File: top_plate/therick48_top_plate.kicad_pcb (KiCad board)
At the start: 2 copper layers, 227.2 x 75.2 mm, 54 parts, among them U1 HOLE, U10 HOLE, U11 HOLE, U12 HOLE, U13 HOLE, U14 HOLE, U15 HOLE, U16 HOLE, U17 HOLE, U18 HOLE, U19 HOLE, U2 HOLE, U20 HOLE, U21 HOLE, U22 HOLE, U23 HOLE, U24 HOLE, U25 HOLE, U26 HOLE, U27 HOLE, U28 HOLE, U29 HOLE, U3 HOLE, U30 HOLE, U31 HOLE, U32 HOLE, U33 HOLE, U34 HOLE, U35 HOLE, U36 HOLE, U37 HOLE, U38 HOLE, U39 HOLE, U4 HOLE, U40 HOLE, U41 HOLE, U42 HOLE, U43 HOLE, U44 HOLE, U45 HOLE, U46 HOLE, U47 HOLE, U48 HOLE, U5 HOLE, U6 HOLE, U7 HOLE, U8 HOLE, U9 HOLE

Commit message: Add Gerbers
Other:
- board text added: "therick48 Rev 1.0"
- board text removed: "therick_19mm"
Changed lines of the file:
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@@
   )
   (gr_line (start 273.6 38.38) (end 273.6 106.78) (layer Edge.Cuts) (width 0.05))
-  (gr_text therick_19mm (at 254.98 91.58) (layer B.SilkS)
+  (gr_text "therick48 Rev 1.0" (at 254.98 91.58) (layer B.SilkS)
     (effects (font (size 1.5 1.5) (thickness 0.2)) (justify mirror))
   )

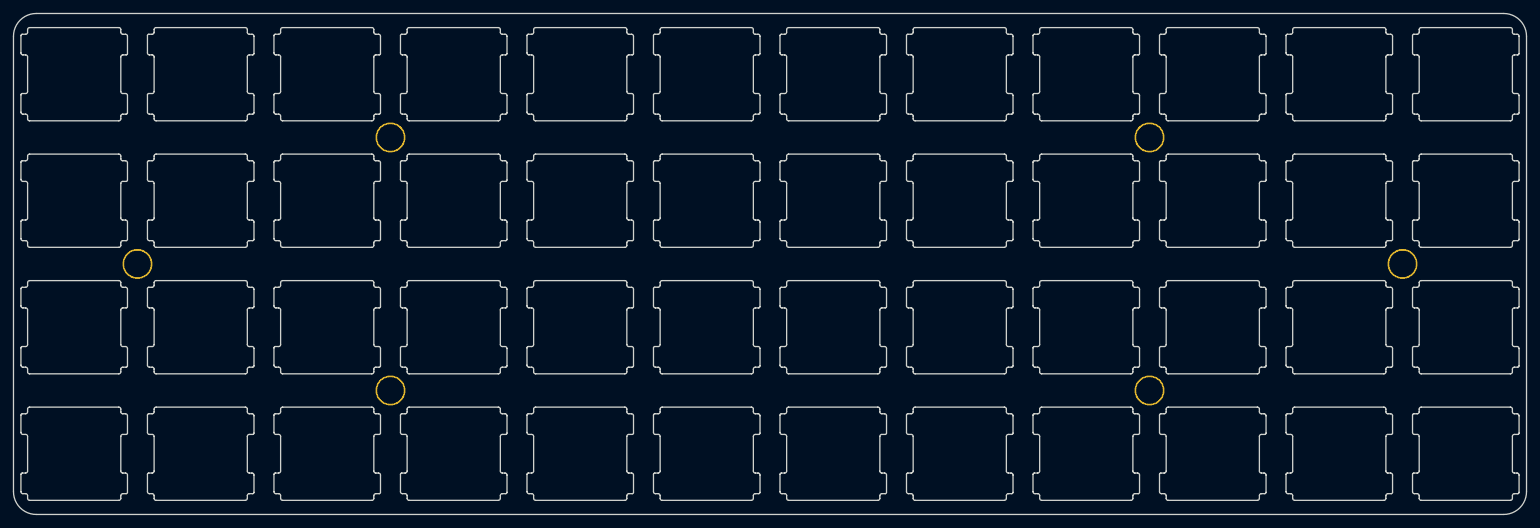
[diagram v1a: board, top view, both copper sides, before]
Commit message: Updated mounting holes
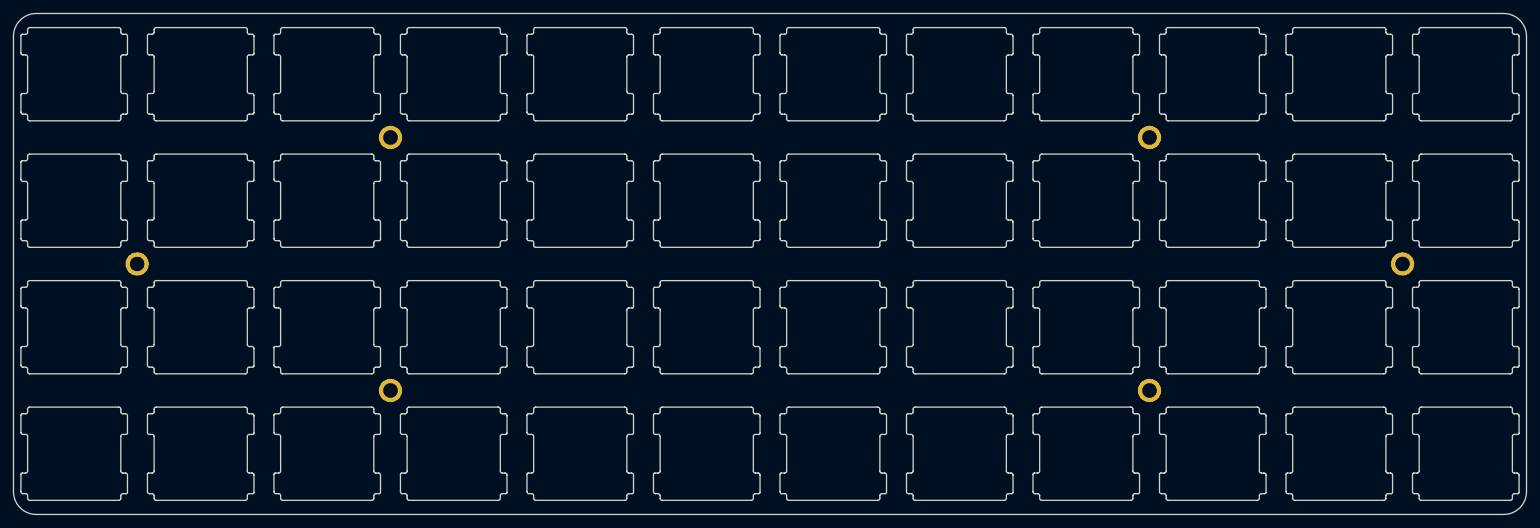
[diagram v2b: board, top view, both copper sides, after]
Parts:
- H1, H2, H3, H4, H5, H6: footprint random-keyboard-parts:plate_hole_4mm_tht -> random-keyboard-parts:Generic-Mounthole
- moved H2 2.03 mm to (103.0, 53.6)
- moved H4 2.03 mm to (217.0, 53.6)
- moved H3 2.03 mm to (103.0, 91.6)
- moved H5 2.03 mm to (217.0, 91.6)
- moved H6 2.03 mm to (255.0, 72.6)
- moved H1 2.03 mm to (64.9, 72.6)
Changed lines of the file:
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@@
     (solder_mask_min_width 0.25)
     (aux_axis_origin 0 0)
-    (visible_elements FFFFEF7F)
+    (visible_elements FFFFFF7F)
     (pcbplotparams
       (layerselection 0x010fc_ffffffff)
@@
     (uvia_drill 0.1)
   )
+  (module random-keyboard-parts:Generic-Mounthole locked (layer F.Cu)
+    (at 254.98 72.58)
+    (attr virtual)
+    (fp_text reference H6 (at 0 2) (layer Dwgs.User)
+      (effects (font (size 1 1) (thickness 0.15)))
+    )
+    (fp_text value MountingHole (at 0 -2) (layer Dwgs.User)
+      (effects (font (size 1 1) (thickness 0.15)))
+    )
+    (pad 1 thru_hole circle (at 0 0) (size 3.5 3.5) (drill 2.2) (layers *.Cu *.Mask))
+  )
+  (module random-keyboard-parts:Generic-Mounthole locked (layer F.Cu)
+    (at 216.98 91.58)
+    (attr virtual)
+    (fp_text reference H5 (at 0 2) (layer Dwgs.User)
+      (effects (font (size 1 1) (thickness 0.15)))
+    )
+    (fp_text value MountingHole (at 0 -2) (layer Dwgs.User)
+      (effects (font (size 1 1) (thickness 0.15)))
+    )
+    (pad 1 thru_hole circle (at 0 0) (size 3.5 3.5) (drill 2.2) (layers *.Cu *.Mask))
+  )
+  (module random-keyboard-parts:Generic-Mounthole locked (layer F.Cu)
+    (at 216.98 53.58)
+    (attr virtual)
+    (fp_text reference H4 (at 0 2) (layer Dwgs.User)
+      (effects (font (size 1 1) (thickness 0.15)))
+    )
+    (fp_text value MountingHole (at 0 -2) (layer Dwgs.User)
+      (effects (font (size 1 1) (thickness 0.15)))
+    )
+    (pad 1 thru_hole circle (at 0 0) (size 3.5 3.5) (drill 2.2) (layers *.Cu *.Mask))
+  )
+  (module random-keyboard-parts:Generic-Mounthole locked (layer F.Cu)
+    (at 102.98 91.58)
+    (attr virtual)
+    (fp_text reference H3 (at 0 2) (layer Dwgs.User)
+      (effects (font (size 1 1) (thickness 0.15)))
+    )
+    (fp_text value MountingHole (at 0 -2) (layer Dwgs.User)
+      (effects (font (size 1 1) (thickness 0.15)))
+    )
+    (pad 1 thru_hole circle (at 0 0) (size 3.5 3.5) (drill 2.2) (layers *.Cu *.Mask))
+  )
+  (module random-keyboard-parts:Generic-Mounthole locked (layer F.Cu)
+    (at 102.98 53.58)
+    (attr virtual)
+    (fp_text reference H2 (at 0 2) (layer Dwgs.User)
+      (effects (font (size 1 1) (thickness 0.15)))
+    )
+    (fp_text value MountingHole (at 0 -2) (layer Dwgs.User)
+      (effects (font (size 1 1) (thickness 0.15)))
+    )
+    (pad 1 thru_hole circle (at 0 0) (size 3.5 3.5) (drill 2.2) (layers *.Cu *.Mask))
+  )
+  (module random-keyboard-parts:Generic-Mounthole locked (layer F.Cu)
+    (at 64.9292 72.58)
+    (attr virtual)
+    (fp_text reference H1 (at 0 2) (layer Dwgs.User)
+      (effects (font (size 1 1) (thickness 0.15)))
+    )
+    (fp_text value MountingHole (at 0 -2) (layer Dwgs.User)
+      (effects (font (size 1 1) (thickness 0.15)))
+    )
+    (pad 1 thru_hole circle (at 0 0) (size 3.5 3.5) (drill 2.2) (layers *.Cu *.Mask))
+  )
   (module random-keyboard-parts:MX100_slot (layer F.Cu)
     (at 264.48 63.08)
@@
     (fp_arc (start -7.8 -5.8) (end -7.8 -6) (angle -90) (layer Edge.Cuts) (width 0.1))
   )
-  (module random-keyboard-parts:plate_hole_4mm_tht locked (layer F.Cu)
-    (at 64.9292 74.612)
-    (fp_text reference H1 (at 0 1.1811) (layer Dwgs.User)
-      (effects (font (size 1 1) (thickness 0.15)))
-    )
-    (fp_text value MountingHole (at 0 -0.5) (layer F.Fab)
-      (effects (font (size 1 1) (thickness 0.15)))
-    )
-    (pad 1 thru_hole circle (at 0.0508 -2.032) (size 4.5 4.5) (drill 4) (layers *.Cu *.Mask))
-  )
-  (module random-keyboard-parts:plate_hole_4mm_tht locked (layer F.Cu)
-    (at 102.9292 55.612)
-    (fp_text reference H2 (at 0 1.1811) (layer Dwgs.User)
-      (effects (font (size 1 1) (thickness 0.15)))
-    )
-    (fp_text value MountingHole (at 0 -0.5) (layer F.Fab)
-      (effects (font (size 1 1) (thickness 0.15)))
-    )
-    (pad 1 thru_hole circle (at 0.0508 -2.032) (size 4.5 4.5) (drill 4) (layers *.Cu *.Mask))
-  )
-  (module random-keyboard-parts:plate_hole_4mm_tht locked (layer F.Cu)
-    (at 102.9292 93.612)
-    (fp_text reference H3 (at 0 1.1811) (layer Dwgs.User)
-      (effects (font (size 1 1) (thickness 0.15)))
-    )
-    (fp_text value MountingHole (at 0 -0.5) (layer F.Fab)
-      (effects (font (size 1 1) (thickness 0.15)))
-    )
-    (pad 1 thru_hole circle (at 0.0508 -2.032) (size 4.5 4.5) (drill 4) (layers *.Cu *.Mask))
-  )
-  (module random-keyboard-parts:plate_hole_4mm_tht locked (layer F.Cu)
-    (at 216.9292 55.612)
-    (fp_text reference H4 (at 0 1.1811) (layer Dwgs.User)
-      (effects (font (size 1 1) (thickness 0.15)))
-    )
-    (fp_text value MountingHole (at 0 -0.5) (layer F.Fab)
-      (effects (font (size 1 1) (thickness 0.15)))
-    )
-    (pad 1 thru_hole circle (at 0.0508 -2.032) (size 4.5 4.5) (drill 4) (layers *.Cu *.Mask))
-  )
-  (module random-keyboard-parts:plate_hole_4mm_tht locked (layer F.Cu)
-    (at 216.9292 93.612)
-    (fp_text reference H5 (at 0 1.1811) (layer Dwgs.User)
-      (effects (font (size 1 1) (thickness 0.15)))
-    )
-    (fp_text value MountingHole (at 0 -0.5) (layer F.Fab)
-      (effects (font (size 1 1) (thickness 0.15)))
-    )
-    (pad 1 thru_hole circle (at 0.0508 -2.032) (size 4.5 4.5) (drill 4) (layers *.Cu *.Mask))
-  )
-  (module random-keyboard-parts:plate_hole_4mm_tht locked (layer F.Cu)
-    (at 254.9292 74.612)
-    (fp_text reference H6 (at 0 1.1811) (layer Dwgs.User)
-      (effects (font (size 1 1) (thickness 0.15)))
-    )
-    (fp_text value MountingHole (at 0 -0.5) (layer F.Fab)
-      (effects (font (size 1 1) (thickness 0.15)))
-    )
-    (pad 1 thru_hole circle (at 0.0508 -2.032) (size 4.5 4.5) (drill 4) (layers *.Cu *.Mask))
-  )
   (gr_line (start 273.6 38.38) (end 273.6 106.78) (layer Edge.Cuts) (width 0.05))

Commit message: Added more mounting holes
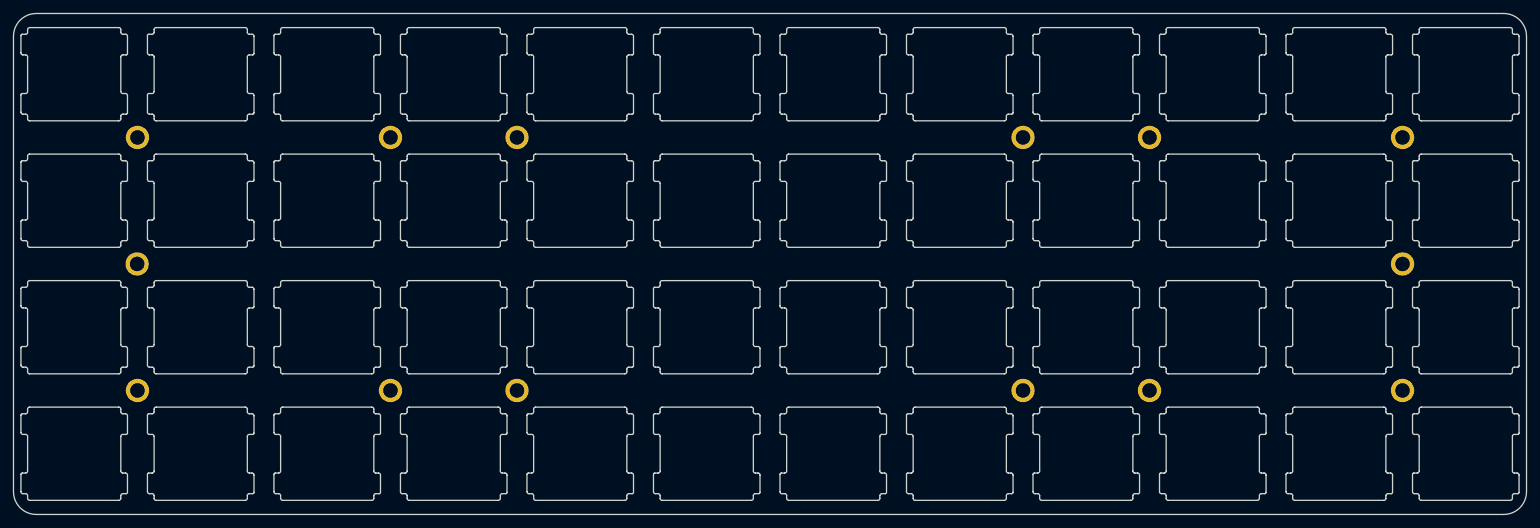
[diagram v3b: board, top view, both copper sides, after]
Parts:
- added H10: MountingHole, random-keyboard-parts:Generic-Mounthole, F.Cu at (122.0, 91.6)
- added H11: MountingHole, random-keyboard-parts:Generic-Mounthole, F.Cu at (198.0, 91.6)
- added H12: MountingHole, random-keyboard-parts:Generic-Mounthole, F.Cu at (198.0, 53.6)
- added H13: MountingHole, random-keyboard-parts:Generic-Mounthole, F.Cu at (255.0, 91.6)
- added H14: MountingHole, random-keyboard-parts:Generic-Mounthole, F.Cu at (255.0, 53.6)
- added H7: MountingHole, random-keyboard-parts:Generic-Mounthole, F.Cu at (65.0, 53.6)
- added H8: MountingHole, random-keyboard-parts:Generic-Mounthole, F.Cu at (65.0, 91.6)
- added H9: MountingHole, random-keyboard-parts:Generic-Mounthole, F.Cu at (122.0, 53.6)
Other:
- board text added: "therick48 Rev 1.1"
- board text removed: "therick48 Rev 1.0"
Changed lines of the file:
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@@
     (tracks 0)
     (zones 0)
-    (modules 54)
+    (modules 62)
     (nets 1)
   )
@@
     (solder_mask_min_width 0.25)
     (aux_axis_origin 0 0)
-    (visible_elements FFFFFF7F)
+    (visible_elements FFFFEF7F)
     (pcbplotparams
       (layerselection 0x010fc_ffffffff)
@@
     (uvia_drill 0.1)
   )
+  (module random-keyboard-parts:Generic-Mounthole (layer F.Cu)
+    (at 254.98 53.58)
+    (attr virtual)
+    (fp_text reference H14 (at 0 2) (layer Dwgs.User)
+      (effects (font (size 1 1) (thickness 0.15)))
+    )
+    (fp_text value MountingHole (at 0 -2) (layer Dwgs.User)
+      (effects (font (size 1 1) (thickness 0.15)))
+    )
+    (pad 1 thru_hole circle (at 0 0) (size 3.5 3.5) (drill 2.2) (layers *.Cu *.Mask))
+  )
+  (module random-keyboard-parts:Generic-Mounthole (layer F.Cu)
+    (at 254.98 91.58)
+    (attr virtual)
+    (fp_text reference H13 (at 0 2) (layer Dwgs.User)
+      (effects (font (size 1 1) (thickness 0.15)))
+    )
+    (fp_text value MountingHole (at 0 -2) (layer Dwgs.User)
+      (effects (font (size 1 1) (thickness 0.15)))
+    )
+    (pad 1 thru_hole circle (at 0 0) (size 3.5 3.5) (drill 2.2) (layers *.Cu *.Mask))
+  )
+  (module random-keyboard-parts:Generic-Mounthole (layer F.Cu)
+    (at 197.98 53.58)
+    (attr virtual)
+    (fp_text reference H12 (at 0 2) (layer Dwgs.User)
+      (effects (font (size 1 1) (thickness 0.15)))
+    )
+    (fp_text value MountingHole (at 0 -2) (layer Dwgs.User)
+      (effects (font (size 1 1) (thickness 0.15)))
+    )
+    (pad 1 thru_hole circle (at 0 0) (size 3.5 3.5) (drill 2.2) (layers *.Cu *.Mask))
+  )
+  (module random-keyboard-parts:Generic-Mounthole (layer F.Cu)
+    (at 197.98 91.58)
+    (attr virtual)
+    (fp_text reference H11 (at 0 2) (layer Dwgs.User)
+      (effects (font (size 1 1) (thickness 0.15)))
+    )
+    (fp_text value MountingHole (at 0 -2) (layer Dwgs.User)
+      (effects (font (size 1 1) (thickness 0.15)))
+    )
+    (pad 1 thru_hole circle (at 0 0) (size 3.5 3.5) (drill 2.2) (layers *.Cu *.Mask))
+  )
+  (module random-keyboard-parts:Generic-Mounthole (layer F.Cu)
+    (at 121.98 91.58)
+    (attr virtual)
+    (fp_text reference H10 (at 0 2) (layer Dwgs.User)
+      (effects (font (size 1 1) (thickness 0.15)))
+    )
+    (fp_text value MountingHole (at 0 -2) (layer Dwgs.User)
+      (effects (font (size 1 1) (thickness 0.15)))
+    )
+    (pad 1 thru_hole circle (at 0 0) (size 3.5 3.5) (drill 2.2) (layers *.Cu *.Mask))
+  )
+  (module random-keyboard-parts:Generic-Mounthole (layer F.Cu)
+    (at 121.98 53.58)
+    (attr virtual)
+    (fp_text reference H9 (at 0 2) (layer Dwgs.User)
+      (effects (font (size 1 1) (thickness 0.15)))
+    )
+    (fp_text value MountingHole (at 0 -2) (layer Dwgs.User)
+      (effects (font (size 1 1) (thickness 0.15)))
+    )
+    (pad 1 thru_hole circle (at 0 0) (size 3.5 3.5) (drill 2.2) (layers *.Cu *.Mask))
+  )
+  (module random-keyboard-parts:Generic-Mounthole (layer F.Cu)
+    (at 64.98 91.58)
+    (attr virtual)
+    (fp_text reference H8 (at 0 2) (layer Dwgs.User)
+      (effects (font (size 1 1) (thickness 0.15)))
+    )
+    (fp_text value MountingHole (at 0 -2) (layer Dwgs.User)
+      (effects (font (size 1 1) (thickness 0.15)))
+    )
+    (pad 1 thru_hole circle (at 0 0) (size 3.5 3.5) (drill 2.2) (layers *.Cu *.Mask))
+  )
+  (module random-keyboard-parts:Generic-Mounthole (layer F.Cu)
+    (at 64.98 53.58)
+    (attr virtual)
+    (fp_text reference H7 (at 0 2) (layer Dwgs.User)
+      (effects (font (size 1 1) (thickness 0.15)))
+    )
+    (fp_text value MountingHole (at 0 -2) (layer Dwgs.User)
+      (effects (font (size 1 1) (thickness 0.15)))
+    )
+    (pad 1 thru_hole circle (at 0 0) (size 3.5 3.5) (drill 2.2) (layers *.Cu *.Mask))
+  )
   (module random-keyboard-parts:Generic-Mounthole locked (layer F.Cu)
     (at 254.98 72.58)
@@
   )
   (gr_line (start 273.6 38.38) (end 273.6 106.78) (layer Edge.Cuts) (width 0.05))
-  (gr_text "therick48 Rev 1.0" (at 254.98 91.58) (layer B.SilkS)
+  (gr_text "therick48 Rev 1.1" (at 238.26 91.58) (layer B.SilkS)
     (effects (font (size 1.5 1.5) (thickness 0.2)) (justify mirror))
   )
@@
   (gr_arc (start 270.18 38.38) (end 273.6 38.38) (angle -90) (layer Edge.Cuts) (width 0.05))
   (gr_arc (start 270.18 106.78) (end 270.18 110.2) (angle -90) (layer Edge.Cuts) (width 0.05))
-  (gr_text JLCJLCJLCJLC (at 64.98 91.58) (layer B.SilkS)
+  (gr_text JLCJLCJLCJLC (at 76.38 91.58) (layer B.SilkS)
     (effects (font (size 1 1) (thickness 0.15)) (justify mirror))
   )

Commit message: Move mounting holes to PCB
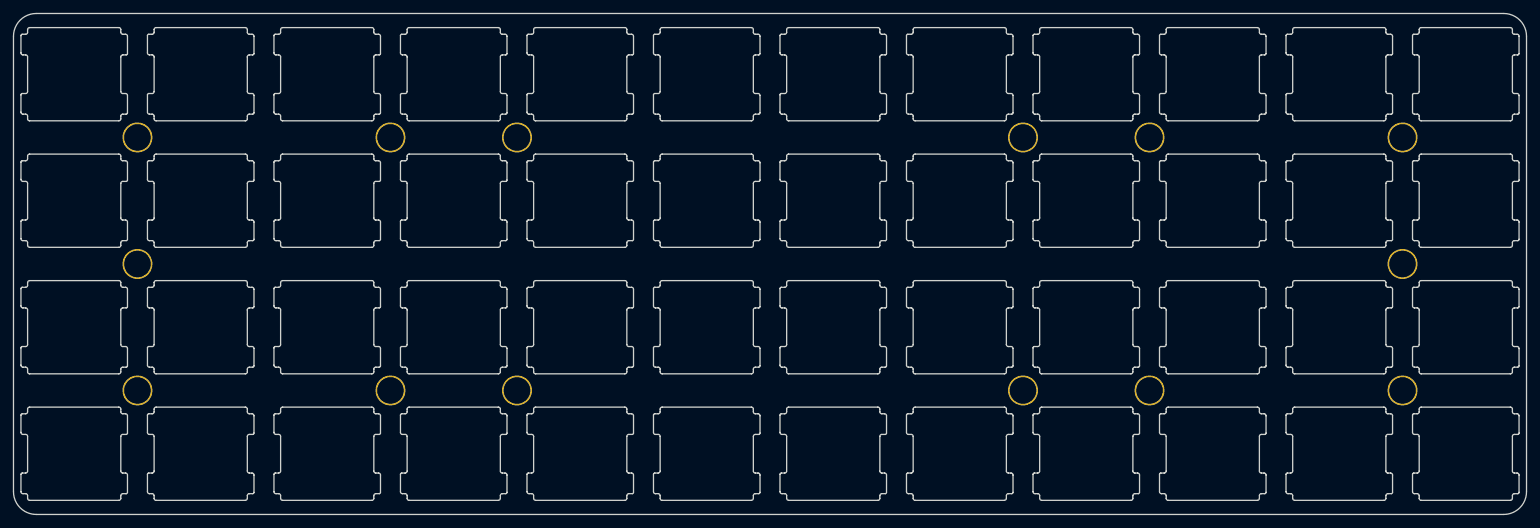
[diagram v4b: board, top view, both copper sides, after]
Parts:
- H1, H10, H11, H12, H13, H14, H2, H3, H4, H5, H6, H7, H8, H9: footprint random-keyboard-parts:Generic-Mounthole -> random-keyboard-parts:plate_hole_4mm_tht
- moved H2 2.03 mm to (102.9, 55.6)
- moved H7 2.03 mm to (64.9, 55.6)
- moved H9 2.03 mm to (121.9, 55.6)
- moved H12 2.03 mm to (197.9, 55.6)
- moved H14 2.03 mm to (254.9, 55.6)
- moved H4 2.03 mm to (216.9, 55.6)
- moved H10 2.03 mm to (121.9, 93.6)
- moved H3 2.03 mm to (102.9, 93.6)
- moved H8 2.03 mm to (64.9, 93.6)
- moved H11 2.03 mm to (197.9, 93.6)
- moved H13 2.03 mm to (254.9, 93.6)
- moved H5 2.03 mm to (216.9, 93.6)
- moved H6 2.03 mm to (254.9, 74.6)
- moved H1 2.03 mm to (64.9, 74.6)
